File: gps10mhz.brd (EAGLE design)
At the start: 100 x 80 mm, 28 parts, among them IC2 7803.3, IC3 CD74HC132E, U1 BB3553AM

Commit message: up
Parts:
- added C13, C14, C15, C16: 0.01uf, rcl:C0805
- moved LED1 34.7 mm to (50.8, 5.08)
- moved SV2 30.0 mm to (64.8, 43.2), turned to 90 degrees
- moved TP1 29.0 mm to (34.3, 59.7)
- moved C12 25.4 mm to (48.3, 57.1)
- moved IC3 25.4 mm to (48.3, 44.5)
- moved C10 25.0 mm to (54.6, 57.1)
- moved C8 23.6 mm to (35.6, 50.8)
- moved TP5 23.6 mm to (64.8, 33.0)
- moved TP4 23.3 mm to (26.7, 59.7)
- moved TP3 22.7 mm to (26.7, 54.6)
- moved R3 22.2 mm to (35.6, 47.0)
- moved R4 18.9 mm to (41.9, 57.1)
- moved C11 15.2 mm to (64.8, 6.35)
- moved R5 13.1 mm to (69.8, 10.2)
- moved C9 11.4 mm to (69.8, 6.35)
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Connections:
- net +15V: now also C14.1
- net -15V: now also C13.1
- net 0V: now also C13.2, C14.2
- net 10MHZ_IN: now also C15.2
- net 10MHZ_OUT: now also C16.1
- net IN: now also C15.1
- net OUT: now also C16.2
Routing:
- net +3V3: track 141.1 -> 101.4 mm
- net 10MHZ_OUT: track 57.8 -> 37.6 mm, vias 1 -> 0
- net N$1: track 5.14 -> 21.1 mm, vias 0 -> 1
- net 0V: track 6.46 -> 21.3 mm
- net N$2: track 36.4 -> 22.3 mm
- net TTL: track 30.3 -> 42.1 mm
- net SINE_IN: track 26.8 -> 36.8 mm
- net -15V: track 47.2 -> 52.5 mm
- net N$4: track 19.9 -> 16.2 mm
- net N$3: track 29.2 -> 25.7 mm
- net +15V: track 88.5 -> 85.5 mm
- net 10MHZ_IN: track 17.0 -> 19.5 mm
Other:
- board size 100 x 80 mm -> 86 x 72.4 mm

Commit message: up
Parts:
- moved TP1 12.0 mm to (40.6, 49.5)
- turned R4 to 180 degrees
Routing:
- net SINE_IN: track 36.8 -> 21.2 mm, vias 0 -> 1
- net +3V3: track 101.4 -> 102.4 mm
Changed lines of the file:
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@@
 <attribute name="VALUE" x="35.56" y="43.18" size="1.27" layer="27"/>
 </element>
-<element name="R4" library="rcl" library_urn="urn:adsk.eagle:library:334" package="R1206" package3d_urn="urn:adsk.eagle:package:23540/2" value="1000" x="41.91" y="57.15" smashed="yes">
-<attribute name="NAME" x="40.64" y="58.42" size="1.27" layer="25"/>
-<attribute name="POPULARITY" value="19" x="41.91" y="57.15" size="1.778" layer="27" display="off"/>
-<attribute name="SPICEPREFIX" value="R" x="41.91" y="57.15" size="1.778" layer="27" display="off"/>
-<attribute name="VALUE" x="40.64" y="54.61" size="1.27" layer="27"/>
-</element>
-<element name="TP1" library="testpad" library_urn="urn:adsk.eagle:library:385" package="P1-13" package3d_urn="urn:adsk.eagle:package:27946/1" value="PTR1PAD1-13" x="34.29" y="59.69" smashed="yes">
-<attribute name="NAME" x="35.814" y="59.69" size="1.27" layer="25" ratio="10"/>
-<attribute name="POPULARITY" value="2" x="34.29" y="59.69" size="1.778" layer="27" display="off"/>
-<attribute name="TP_SIGNAL_NAME" value="" x="34.29" y="59.69" size="1.778" layer="27" display="off"/>
-<attribute name="VALUE" x="35.56" y="58.42" size="0.0254" layer="27"/>
+<element name="R4" library="rcl" library_urn="urn:adsk.eagle:library:334" package="R1206" package3d_urn="urn:adsk.eagle:package:23540/2" value="1000" x="41.91" y="57.15" smashed="yes" rot="R180">
+<attribute name="NAME" x="43.18" y="55.88" size="1.27" layer="25" rot="R180"/>
+<attribute name="POPULARITY" value="19" x="41.91" y="57.15" size="1.778" layer="27" rot="R180" display="off"/>
+<attribute name="SPICEPREFIX" value="R" x="41.91" y="57.15" size="1.778" layer="27" rot="R180" display="off"/>
+<attribute name="VALUE" x="43.18" y="59.69" size="1.27" layer="27" rot="R180"/>
+</element>
+<element name="TP1" library="testpad" library_urn="urn:adsk.eagle:library:385" package="P1-13" package3d_urn="urn:adsk.eagle:package:27946/1" value="PTR1PAD1-13" x="40.64" y="49.53" smashed="yes">
+<attribute name="NAME" x="42.164" y="49.53" size="1.27" layer="25" ratio="10"/>
+<attribute name="POPULARITY" value="2" x="40.64" y="49.53" size="1.778" layer="27" display="off"/>
+<attribute name="TP_SIGNAL_NAME" value="" x="40.64" y="49.53" size="1.778" layer="27" display="off"/>
+<attribute name="VALUE" x="41.91" y="48.26" size="0.0254" layer="27"/>
 </element>
 <element name="TP2" library="testpad" library_urn="urn:adsk.eagle:library:385" package="P1-13" package3d_urn="urn:adsk.eagle:package:27946/1" value="PTR1PAD1-13" x="5.08" y="46.99" smashed="yes">
@@
 <wire x1="47.4726" y1="55.626" x2="47.5488" y2="55.5498" width="0.762" layer="1"/>
 <wire x1="47.4726" y1="55.626" x2="47.244" y2="55.9308" width="0.762" layer="1"/>
-<wire x1="38.1762" y1="47.0154" x2="37.0332" y2="47.0154" width="0.762" layer="1"/>
-<wire x1="43.1292" y1="51.9684" x2="38.1762" y2="47.0154" width="0.762" layer="1"/>
-<wire x1="43.9674" y1="51.9684" x2="43.1292" y2="51.9684" width="0.762" layer="1"/>
+<wire x1="37.0332" y1="48.4632" x2="37.0332" y2="47.0154" width="0.762" layer="1"/>
+<wire x1="38.7096" y1="50.1396" x2="37.0332" y2="48.4632" width="0.762" layer="1"/>
+<wire x1="38.7096" y1="50.3682" x2="38.7096" y2="50.1396" width="0.762" layer="1"/>
+<wire x1="40.3098" y1="51.9684" x2="38.7096" y2="50.3682" width="0.762" layer="1"/>
+<wire x1="43.9674" y1="51.9684" x2="40.3098" y2="51.9684" width="0.762" layer="1"/>
 <wire x1="37.0332" y1="47.0154" x2="36.982" y2="46.99" width="0.762" layer="1"/>
 <wire x1="43.9674" y1="51.9684" x2="44.29" y2="52.07" width="0.762" layer="1"/>
@@
 <wire x1="66.04" y1="48.26" x2="67.818" y2="46.482" width="0.762" layer="16"/>
 </signal>
-<signal name="SINE_IN">
+<signal name="SINE_IN" class="2">
 <contactref element="C8" pad="1"/>
 <contactref element="R3" pad="1"/>
@@
 <contactref element="TP1" pad="TP"/>
 <contactref element="IC3" pad="2"/>
-<wire x1="36.4998" y1="50.0634" x2="36.4998" y2="50.7492" width="0.1524" layer="1"/>
-<wire x1="34.2138" y1="47.7774" x2="36.4998" y2="50.0634" width="0.1524" layer="1"/>
-<wire x1="34.2138" y1="47.0154" x2="34.2138" y2="47.7774" width="0.1524" layer="1"/>
-<wire x1="36.4998" y1="50.7492" x2="36.51" y2="50.8" width="0.1524" layer="1"/>
-<wire x1="34.2138" y1="47.0154" x2="34.138" y2="46.99" width="0.1524" layer="1"/>
-<wire x1="42.8244" y1="57.15" x2="43.332" y2="57.15" width="0.1524" layer="1"/>
-<wire x1="37.719" y1="52.0446" x2="39.9669" y2="54.2925" width="0.1524" layer="1"/>
-<wire x1="39.9669" y1="54.2925" x2="42.8244" y2="57.15" width="0.1524" layer="1"/>
-<wire x1="37.719" y1="51.5112" x2="37.719" y2="52.0446" width="0.1524" layer="1"/>
-<wire x1="37.0332" y1="50.8254" x2="37.719" y2="51.5112" width="0.1524" layer="1"/>
-<wire x1="36.576" y1="50.8254" x2="37.0332" y2="50.8254" width="0.1524" layer="1"/>
-<wire x1="36.576" y1="50.8254" x2="36.51" y2="50.8" width="0.1524" layer="1"/>
-<wire x1="44.2722" y1="49.6824" x2="44.2722" y2="49.53" width="0.1524" layer="16"/>
-<wire x1="34.29" y1="59.6646" x2="44.2722" y2="49.6824" width="0.1524" layer="16"/>
-<wire x1="44.2722" y1="49.53" x2="44.29" y2="49.53" width="0.1524" layer="16"/>
-<wire x1="34.29" y1="59.6646" x2="34.29" y2="59.69" width="0.1524" layer="16"/>
-<wire x1="34.5948" y1="59.6646" x2="39.9669" y2="54.2925" width="0.1524" layer="1"/>
-<wire x1="34.29" y1="59.6646" x2="34.5948" y2="59.6646" width="0.1524" layer="1"/>
-<wire x1="34.29" y1="59.6646" x2="34.29" y2="59.69" width="0.1524" layer="1"/>
+<wire x1="40.64" y1="49.53" x2="44.29" y2="49.53" width="0.762" layer="16"/>
+<wire x1="36.4998" y1="49.6824" x2="36.4998" y2="50.7492" width="0.762" layer="1"/>
+<wire x1="35.5854" y1="48.768" x2="36.4998" y2="49.6824" width="0.762" layer="1"/>
+<wire x1="34.7472" y1="48.768" x2="35.5854" y2="48.768" width="0.762" layer="1"/>
+<wire x1="34.3662" y1="48.387" x2="34.7472" y2="48.768" width="0.762" layer="1"/>
+<wire x1="34.3662" y1="47.1678" x2="34.3662" y2="48.387" width="0.762" layer="1"/>
+<wire x1="34.2138" y1="47.0154" x2="34.3662" y2="47.1678" width="0.762" layer="1"/>
+<wire x1="36.4998" y1="50.7492" x2="36.51" y2="50.8" width="0.762" layer="1"/>
+<wire x1="34.2138" y1="47.0154" x2="34.138" y2="46.99" width="0.762" layer="1"/>
+<wire x1="40.4622" y1="55.8546" x2="40.4622" y2="57.15" width="0.762" layer="1"/>
+<wire x1="36.576" y1="51.9684" x2="40.4622" y2="55.8546" width="0.762" layer="1"/>
+<wire x1="36.576" y1="51.1302" x2="36.576" y2="51.9684" width="0.762" layer="1"/>
+<wire x1="40.4622" y1="57.15" x2="40.488" y2="57.15" width="0.762" layer="1"/>
+<wire x1="36.576" y1="51.1302" x2="36.51" y2="50.8" width="0.762" layer="1"/>
+<wire x1="36.7284" y1="49.4538" x2="40.3098" y2="49.4538" width="0.762" layer="16"/>
+<wire x1="40.3098" y1="49.4538" x2="40.64" y2="49.53" width="0.762" layer="16"/>
+<wire x1="36.7284" y1="49.4538" x2="36.4998" y2="49.6824" width="0.762" layer="1"/>
+<via x="36.7284" y="49.4538" extent="1-16" drill="0.35"/>
 </signal>
 <signal name="TTL" class="1">

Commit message: up
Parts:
- added R6: 470, rcl:R1206
- moved R2 2.84 mm to (27.9, 43.2)
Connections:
- net N$2 renamed D1
- net N$3 renamed D2
- net N$4 renamed D3
- net 0V: now also R6.1
- net TTL: now also R6.2
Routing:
- net TTL: track 42.1 -> 46.8 mm
- net D1: track 22.3 -> 26.0 mm, vias 0 -> 1
- net OUT: track 24.9 -> 26.2 mm
- net SINE_IN: track 21.2 -> 20.6 mm, vias 1 -> 0
- net +3V3: track 102.4 -> 102.8 mm, vias 0 -> 1
- added copper zone on layer 1, net GND

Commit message: up
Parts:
- added C17: 10uf, rcl:C0805
- added C18, C20, C21: 1000pf, rcl:C0805
- added C19: 0.1uf, rcl:C0805
- added R7: 100, rcl:R1206
- C10: value 0.1uf -> 1000pf
- C12: value 10uf -> 0.1uf
- moved R4 6.35 mm to (35.6, 57.1), turned to 0 degrees
- moved C14 1.27 mm to (29.2, 33.0)
- moved C8 1.27 mm to (35.6, 49.5)
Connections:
- new net BIASV: C18.1, C19.1, R3.2, R7.2
- net +15V: now also C21.1
- net +3V3: now also C17.1, R7.1; no longer R3.2
- net -15V: now also C20.1
- net 0V: now also C17.2, C18.2, C19.2, C20.2, C21.2
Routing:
- net BIASV: track 0.00 -> 13.9 mm, vias 0 -> 2
- net +3V3: track 102.8 -> 94.6 mm, vias 1 -> 0
- net D1: track 26.0 -> 22.3 mm, vias 1 -> 0
- net D2: track 25.7 -> 22.8 mm
- net 0V: track 21.3 -> 23.7 mm, vias 0 -> 19
- net TTL: track 46.8 -> 45.0 mm
- net OUT: track 26.2 -> 24.8 mm, vias 1 -> 0
- net SINE_IN: track 20.6 -> 21.6 mm, vias 0 -> 1
- net -15V: track 52.5 -> 53.3 mm
- net +15V: track 85.5 -> 86.2 mm
- net 10MHZ_OUT: track 37.6 -> 38.1 mm
- net D3: track 16.2 -> 16.7 mm
- added copper zone on layer 16, net 0V
- removed copper zone on layer 1, net GND

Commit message: up
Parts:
- added C22: 10uf, rcl:C0805
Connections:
- net 0V: now also C22.2
- net BIASV: now also C22.1
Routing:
- net BIASV: track 13.9 -> 19.5 mm
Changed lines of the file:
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@@
 <attribute name="VALUE" x="30.48" y="27.94" size="1.27" layer="28" rot="MR0"/>
+</element>
+<element name="C22" library="rcl" library_urn="urn:adsk.eagle:library:334" package="C0805" package3d_urn="urn:adsk.eagle:package:23617/2" value="10uf" x="35.56" y="44.45" smashed="yes" rot="MR0">
+<attribute name="NAME" x="36.83" y="45.72" size="1.27" layer="26" rot="MR0"/>
+<attribute name="POPULARITY" value="63" x="35.56" y="44.45" size="1.778" layer="28" rot="MR0" display="off"/>
+<attribute name="SPICEPREFIX" value="C" x="35.56" y="44.45" size="1.778" layer="28" rot="MR0" display="off"/>
+<attribute name="VALUE" x="36.83" y="41.91" size="1.27" layer="28" rot="MR0"/>
 </element>
 </elements>
@@
 <via x="38.1" y="34.29" extent="1-16" drill="0.35" locked="yes"/>
 <via x="22.86" y="34.29" extent="1-16" drill="0.35" locked="yes"/>
+<contactref element="C22" pad="2"/>
 </signal>
 <signal name="+15V" class="2">
@@
 <wire x1="37.0332" y1="47.3202" x2="37.0332" y2="47.0154" width="0.762" layer="1"/>
 <wire x1="38.1" y1="48.387" x2="37.0332" y2="47.3202" width="0.762" layer="1"/>
-<wire x1="38.1" y1="51.5112" x2="38.1" y2="48.387" width="0.762" layer="16"/>
+<wire x1="38.1" y1="51.5112" x2="38.1" y2="48.9204" width="0.762" layer="16"/>
+<wire x1="38.1" y1="48.9204" x2="38.1" y2="48.387" width="0.762" layer="16"/>
 <wire x1="37.8714" y1="51.7398" x2="38.1" y2="51.5112" width="0.762" layer="16"/>
 <wire x1="37.7952" y1="51.816" x2="37.8714" y2="51.7398" width="0.762" layer="1"/>
@@
 <via x="38.1" y="48.387" extent="1-16" drill="0.35"/>
 <via x="37.8714" y="51.7398" extent="1-16" drill="0.35"/>
+<contactref element="C22" pad="1"/>
+<wire x1="36.4998" y1="48.1584" x2="36.4998" y2="44.5008" width="0.762" layer="16"/>
+<wire x1="37.2618" y1="48.9204" x2="36.4998" y2="48.1584" width="0.762" layer="16"/>
+<wire x1="38.1" y1="48.9204" x2="37.2618" y2="48.9204" width="0.762" layer="16"/>
+<wire x1="36.4998" y1="44.5008" x2="36.51" y2="44.45" width="0.762" layer="16"/>
 </signal>
 </signals>

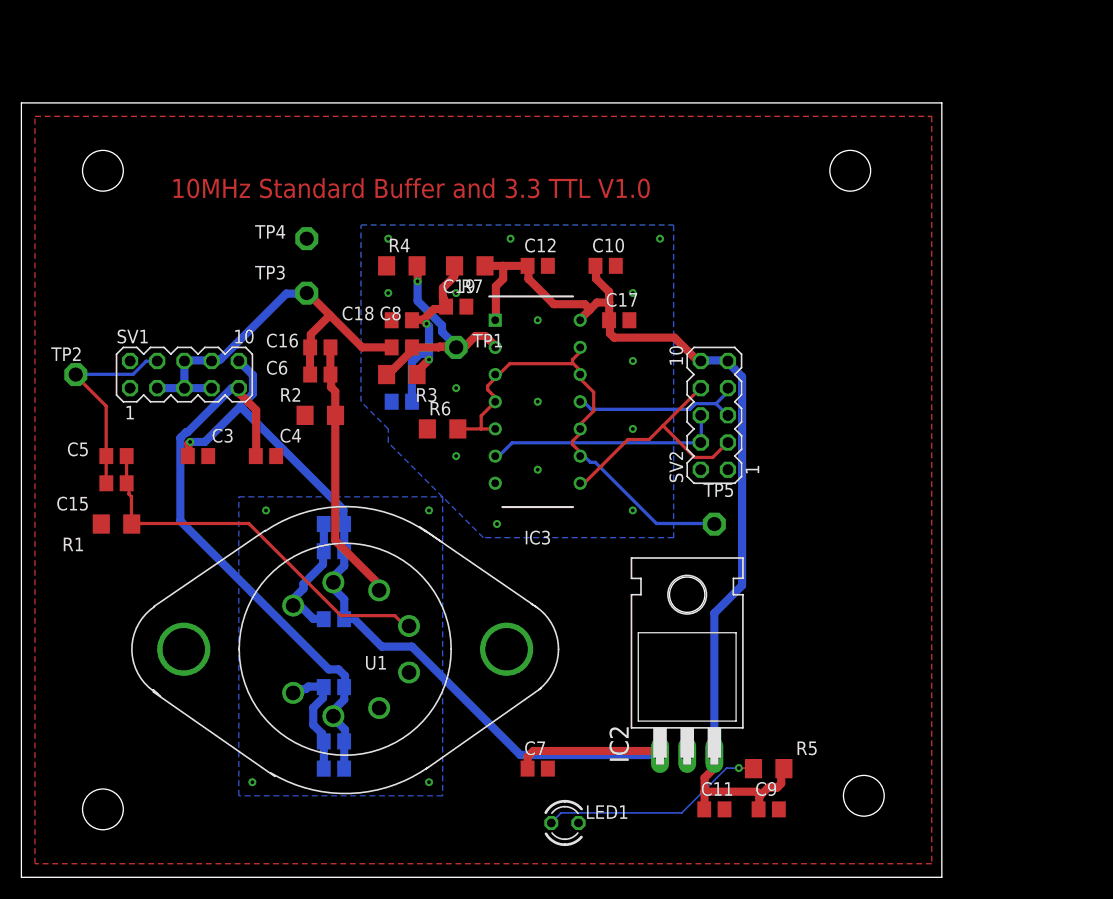
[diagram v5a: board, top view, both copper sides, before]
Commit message: 3.3 digital only version
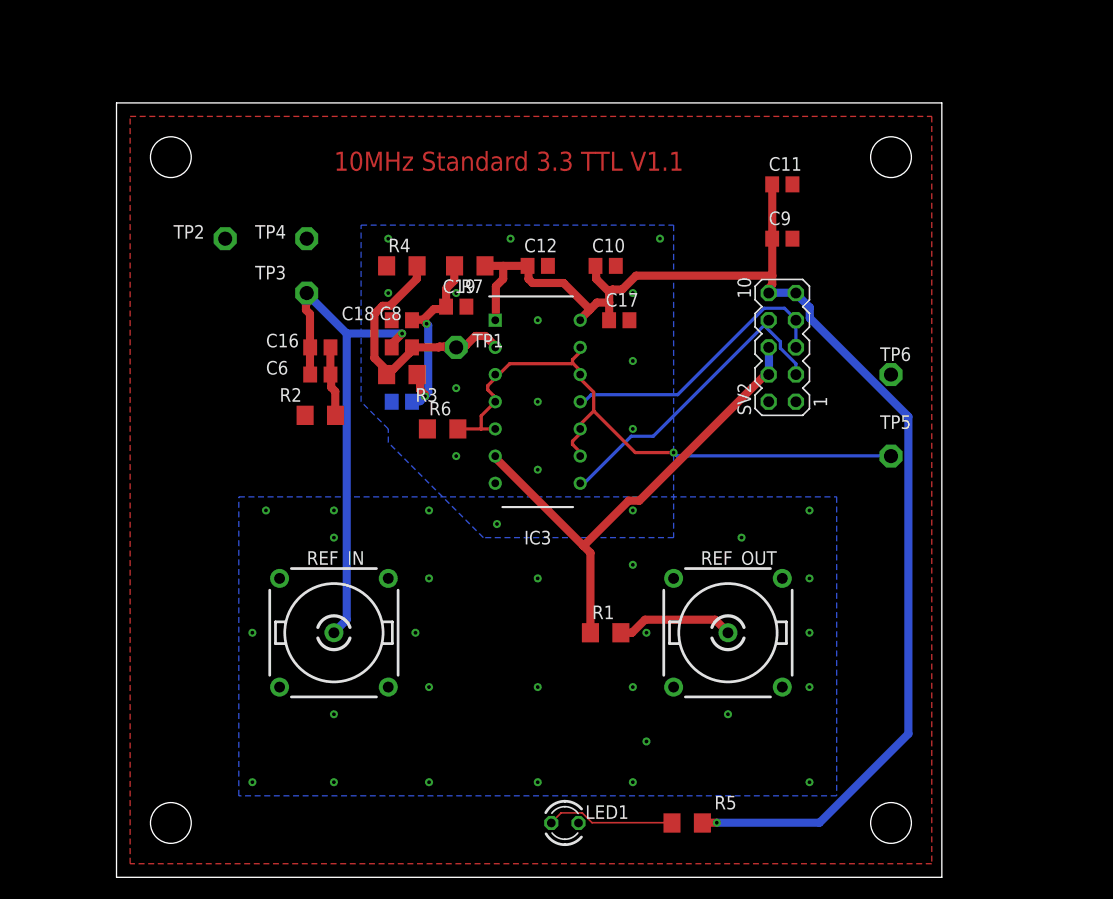
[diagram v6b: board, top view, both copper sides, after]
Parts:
- removed C1, C2, C5, C7: 0.1uf, rcl:C0805
- removed C13, C14, C15: 0.01uf, rcl:C0805
- removed C20, C21: 1000pf, rcl:C0805
- removed C3, C4: 10uf, rcl:C0805
- removed IC2: 7803.3, linear:TO220H
- removed SV1: IO_PWR, con-lstb:MA05-2
- removed U1: BB3553AM, 2025-01-01_18-24-55_Library:LMF8_TEX
- added REF_IN, REF_OUT: A1944-50, con-coax:A1944
- added TP6: PTR1PAD1-13, testpad:P1-13
- R1: value 1000 -> 56
- moved C11 58.8 mm to (71.1, 64.8)
- moved C9 53.4 mm to (71.1, 59.7)
- moved R1 46.8 mm to (54.6, 22.9)
- moved TP2 18.9 mm to (19.1, 59.7)
- moved TP5 17.7 mm to (81.3, 39.4)
- moved R5 9.16 mm to (62.2, 5.08)
- moved SV2 8.98 mm to (71.1, 49.5)
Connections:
- removed net +15V: C14.1, C2.1, C21.1, C3.1, C7.1, IC2.1, SV1.10, U1.2
- removed net -15V: C1.1, C13.1, C20.1, C4.1, SV1.9, U1.7
- removed net 10MHZ_IN: C15.2, C5.2, SV1.4, TP2.TP
- removed net IN: C15.1, C5.1, R1.2, U1.4
- new net REF_OUT_R: R1.2, REF_OUT.1
- net +3V3: no longer IC2.3
- net 0V: now also REF_IN.2, REF_IN.3, REF_IN.4, REF_IN.5, REF_OUT.2, REF_OUT.3, REF_OUT.4, REF_OUT.5, TP2.TP, TP6.TP; no longer C1.2, C13.2, C14.2, C2.2, C20.2, C21.2, C3.2, C4.2, C7.2, IC2.2, R1.1, SV1.1, SV1.2, U1.1, U1.5, U1.6, U1.8
- net 10MHZ_OUT: now also REF_IN.1; no longer SV1.3, SV1.5, SV1.6, SV1.7, SV1.8
- net D1: now also R1.1
- net OUT: no longer U1.3
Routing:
- net +15V: track 86.2 -> 0.00 mm, vias 1 -> 0
- net -15V: track 53.3 -> 0.00 mm
- net IN: track 36.4 -> 0.00 mm
- net +3V3: track 94.6 -> 123.6 mm, vias 0 -> 1
- net D1: track 22.3 -> 46.7 mm
- net 0V: track 23.7 -> 0.00 mm, vias 19 -> 42
- net 10MHZ_IN: track 19.5 -> 0.00 mm
- net OUT: track 24.8 -> 6.67 mm
- net TTL: track 45.0 -> 59.3 mm, vias 0 -> 1
- net REF_OUT_R: track 0.00 -> 11.1 mm
- net 10MHZ_OUT: track 38.1 -> 48.6 mm, vias 0 -> 1
- net D3: track 16.7 -> 26.8 mm
- net N$1: track 21.1 -> 12.1 mm, vias 1 -> 0
- net D2: track 22.8 -> 30.4 mm
- net SINE_IN: track 21.6 -> 25.1 mm, vias 1 -> 0
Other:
- board size 86 x 72.4 mm -> 77.1 x 72.4 mm
- board text added: "10MHz Standard 3.3 TTL V1.1"
- board text removed: "10MHz Standard Buffer and 3.3 TTL V1.0"

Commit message: up
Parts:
- R1: value 56 -> 22
- R3: value 1000 -> 910
- R7: value 100 -> 130
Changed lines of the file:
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@@
 <attribute name="VALUE" x="36.83" y="52.07" size="1.27" layer="27" rot="R180"/>
 </element>
-<element name="R3" library="rcl" library_urn="urn:adsk.eagle:library:334" package="R1206" package3d_urn="urn:adsk.eagle:package:23540/2" value="1000" x="35.56" y="46.99" smashed="yes">
+<element name="R3" library="rcl" library_urn="urn:adsk.eagle:library:334" package="R1206" package3d_urn="urn:adsk.eagle:package:23540/2" value="910" x="35.56" y="46.99" smashed="yes">
 <attribute name="NAME" x="36.83" y="44.45" size="1.27" layer="25"/>
 <attribute name="POPULARITY" value="19" x="35.56" y="46.99" size="1.778" layer="27" display="off"/>
@@
 <attribute name="VALUE" x="54.61" y="49.53" size="1.27" layer="27"/>
 </element>
-<element name="R7" library="rcl" library_urn="urn:adsk.eagle:library:334" package="R1206" package3d_urn="urn:adsk.eagle:package:23540/2" value="100" x="41.91" y="57.15" smashed="yes" rot="R180">
+<element name="R7" library="rcl" library_urn="urn:adsk.eagle:library:334" package="R1206" package3d_urn="urn:adsk.eagle:package:23540/2" value="130" x="41.91" y="57.15" smashed="yes" rot="R180">
 <attribute name="NAME" x="43.18" y="55.88" size="1.27" layer="25" rot="R180"/>
 <attribute name="POPULARITY" value="19" x="41.91" y="57.15" size="1.778" layer="27" rot="R180" display="off"/>
@@
 <attribute name="VALUE" x="63.5" y="15.24" size="1.27" layer="27"/>
 </element>
-<element name="R1" library="rcl" library_urn="urn:adsk.eagle:library:334" package="R1206" package3d_urn="urn:adsk.eagle:package:23540/2" value="56" x="54.61" y="22.86" smashed="yes">
+<element name="R1" library="rcl" library_urn="urn:adsk.eagle:library:334" package="R1206" package3d_urn="urn:adsk.eagle:package:23540/2" value="22" x="54.61" y="22.86" smashed="yes">
 <attribute name="NAME" x="53.34" y="24.13" size="1.27" layer="25"/>
 <attribute name="POPULARITY" value="19" x="54.61" y="22.86" size="1.778" layer="27" display="off"/>
